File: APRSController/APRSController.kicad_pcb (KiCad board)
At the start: 2 copper layers, 96.5 x 94 mm, 29 parts, among them J1 Conn_01x06, J10 Conn_01x02, J2 Conn_01x02, J3 Conn_01x02, J4 Conn_01x02, J5 Conn_01x02, J6 Conn_01x02, J7 Conn_01x02, J8 Conn_01x02, J9 Conn_01x02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

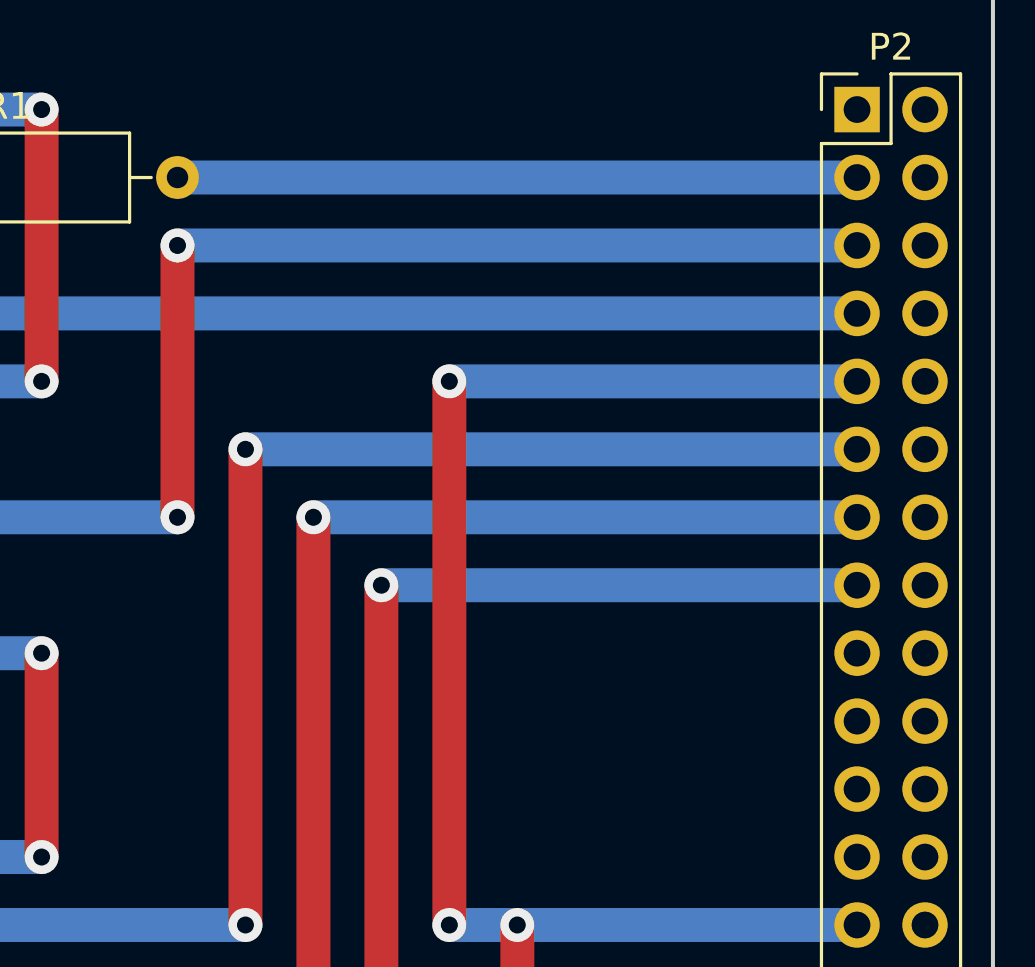
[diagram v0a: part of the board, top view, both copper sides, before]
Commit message: Changed controller circuit so as to avoid the I2C lines on the Pi. PTT is now GPIO10.  First output is now GPIO9.
Added two-tone calibration audio to manual test package.
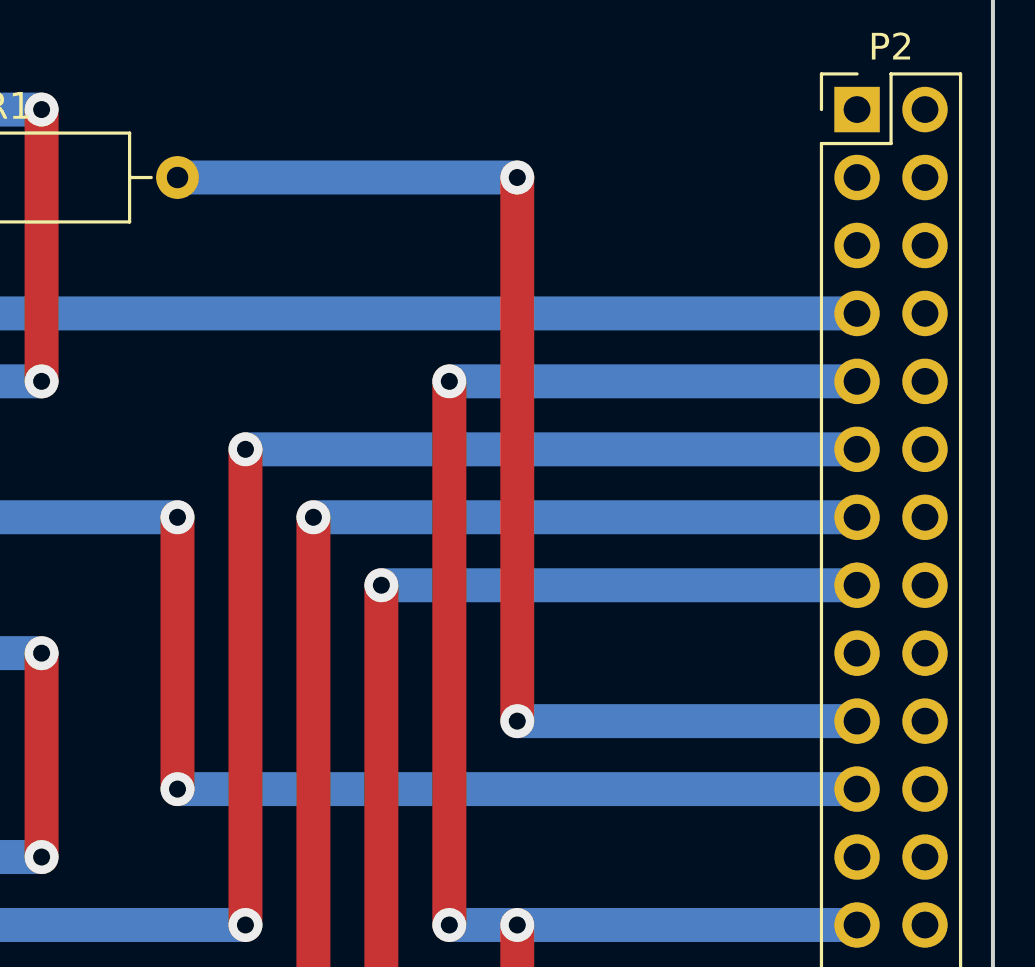
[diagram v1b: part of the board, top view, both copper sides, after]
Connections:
- R1 pad 2: /GPIO2 -> /GPIO10
- R2 pad 2: /GPIO3 -> /GPIO9
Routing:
- net /GPIO9: track 0.00 -> 48.3 mm, vias 0 -> 2
- net /GPIO3: track 48.3 -> 0.00 mm, vias 2 -> 0
- net /GPIO10: track 0.00 -> 45.7 mm, vias 0 -> 2
- net /GPIO2: track 25.4 -> 0.00 mm
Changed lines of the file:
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@@
   (general
     (links 47)
-    (no_connects 0)
-    (area 114.224999 43.104999 211.970334 137.235001)
+    (no_connects 2)
+    (area 114.224999 43.104999 210.895001 137.235001)
     (thickness 1.6)
     (drawings 8)
-    (tracks 152)
+    (tracks 156)
     (zones 0)
     (modules 29)
@@
       (net 45 "Net-(Q2-Pad2)"))
     (pad 2 thru_hole oval (at 12.7 0) (size 1.6 1.6) (drill 0.8) (layers *.Cu *.Mask)
-      (net 43 /GPIO3))
+      (net 42 /GPIO9))
     (model ${KISYS3DMOD}/Resistors_THT.3dshapes/R_Axial_DIN0309_L9.0mm_D3.2mm_P12.70mm_Horizontal.wrl
       (at (xyz 0 0 0))
@@
       (net 35 "Net-(Q1-Pad2)"))
     (pad 2 thru_hole oval (at 12.7 0) (size 1.6 1.6) (drill 0.8) (layers *.Cu *.Mask)
-      (net 37 /GPIO2))
+      (net 41 /GPIO10))
     (model ${KISYS3DMOD}/Resistors_THT.3dshapes/R_Axial_DIN0309_L9.0mm_D3.2mm_P12.70mm_Horizontal.wrl
       (at (xyz 0 0 0))
@@
   (segment (start 180.34 124.46) (end 172.72 124.46) (width 1.27) (layer B.Cu) (net 36))
   (via (at 172.72 124.46) (size 1.27) (drill 0.635) (layers F.Cu B.Cu) (net 36))
-  (segment (start 180.34 78.74) (end 205.74 78.74) (width 1.27) (layer B.Cu) (net 37))
   (segment (start 170.18 83.82) (end 205.74 83.82) (width 1.27) (layer B.Cu) (net 38))
+  (via (at 170.18 83.82) (size 1.27) (drill 0.635) (layers F.Cu B.Cu) (net 38))
   (segment (start 170.18 99.06) (end 170.18 83.82) (width 1.27) (layer F.Cu) (net 38))
-  (via (at 170.18 83.82) (size 1.27) (drill 0.635) (layers F.Cu B.Cu) (net 38))
   (via (at 170.18 83.82) (size 1.27) (drill 0.635) (layers F.Cu B.Cu) (net 38))
   (segment (start 167.64 99.06) (end 170.18 99.06) (width 1.27) (layer B.Cu) (net 38))
@@
   (segment (start 167.64 114.3) (end 185.42 114.3) (width 1.27) (layer B.Cu) (net 40))
   (via (at 185.42 114.3) (size 1.27) (drill 0.635) (layers F.Cu B.Cu) (net 40))
-  (segment (start 180.34 81.28) (end 205.74 81.28) (width 1.27) (layer B.Cu) (net 43))
-  (segment (start 180.34 91.44) (end 180.34 81.28) (width 1.27) (layer F.Cu) (net 43))
-  (via (at 180.34 81.28) (size 1.27) (drill 0.635) (layers F.Cu B.Cu) (net 43))
-  (segment (start 167.64 91.44) (end 180.34 91.44) (width 1.27) (layer B.Cu) (net 43))
-  (via (at 180.34 91.44) (size 1.27) (drill 0.635) (layers F.Cu B.Cu) (net 43))
+  (segment (start 193.04 99.06) (end 205.74 99.06) (width 1.27) (layer B.Cu) (net 41))
+  (segment (start 193.04 78.74) (end 193.04 99.06) (width 1.27) (layer F.Cu) (net 41))
+  (via (at 193.04 99.06) (size 1.27) (drill 0.635) (layers F.Cu B.Cu) (net 41))
+  (segment (start 180.34 78.74) (end 193.04 78.74) (width 1.27) (layer B.Cu) (net 41))
+  (via (at 193.04 78.74) (size 1.27) (drill 0.635) (layers F.Cu B.Cu) (net 41))
+  (segment (start 180.34 101.6) (end 205.74 101.6) (width 1.27) (layer B.Cu) (net 42))
+  (segment (start 180.34 91.44) (end 180.34 101.6) (width 1.27) (layer F.Cu) (net 42))
+  (via (at 180.34 101.6) (size 1.27) (drill 0.635) (layers F.Cu B.Cu) (net 42))
+  (segment (start 167.64 91.44) (end 180.34 91.44) (width 1.27) (layer B.Cu) (net 42))
+  (via (at 180.34 91.44) (size 1.27) (drill 0.635) (layers F.Cu B.Cu) (net 42))
   (segment (start 187.96 93.98) (end 205.74 93.98) (width 1.27) (layer B.Cu) (net 44))
   (segment (start 187.96 121.92) (end 187.96 93.98) (width 1.27) (layer F.Cu) (net 44))
